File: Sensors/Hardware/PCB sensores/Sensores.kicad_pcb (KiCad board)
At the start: 2 copper layers, 108 x 129.5 mm, 49 parts, among them J1 Conn_01x02_Female, J2 Conn_01x03, J3 Conn_02x04_Top_Bottom, J4 Conn_01x02_Female, Q1 2N3904, U1 LM324, U2 LM324, U3 ADP1101, U4 MPX10DP, U5 LM358

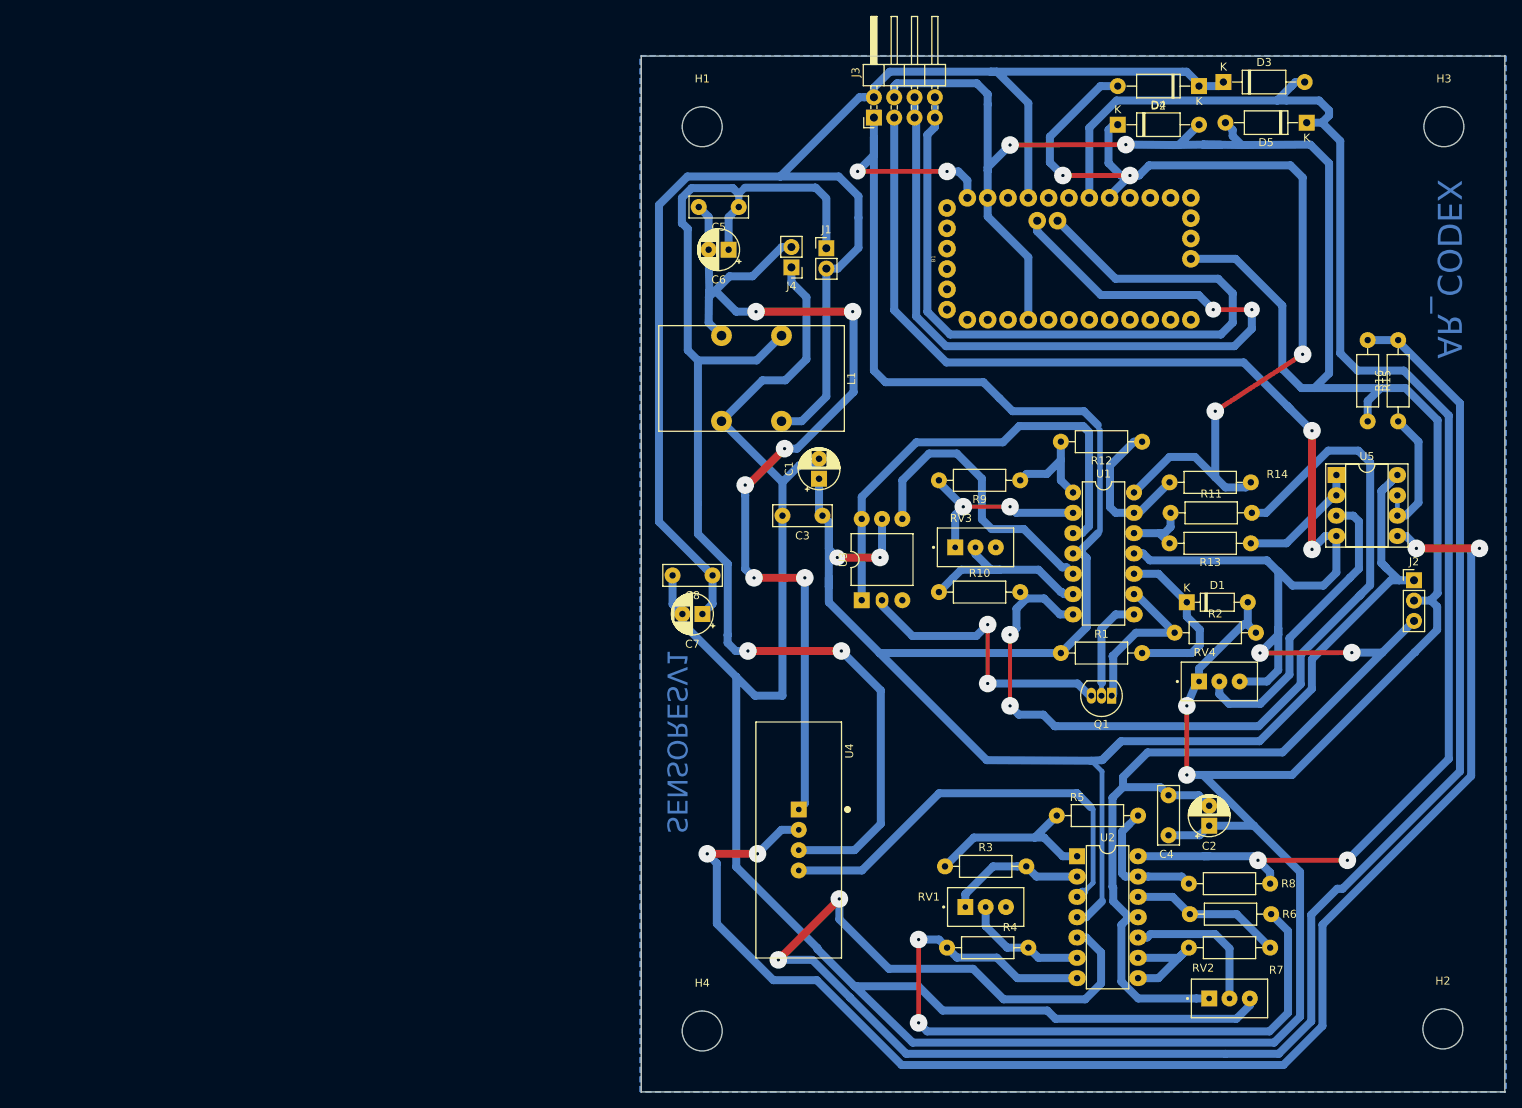
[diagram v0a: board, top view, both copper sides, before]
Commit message: Wrapping everything up. Sensors now work fine. Preliminary PID tunning.
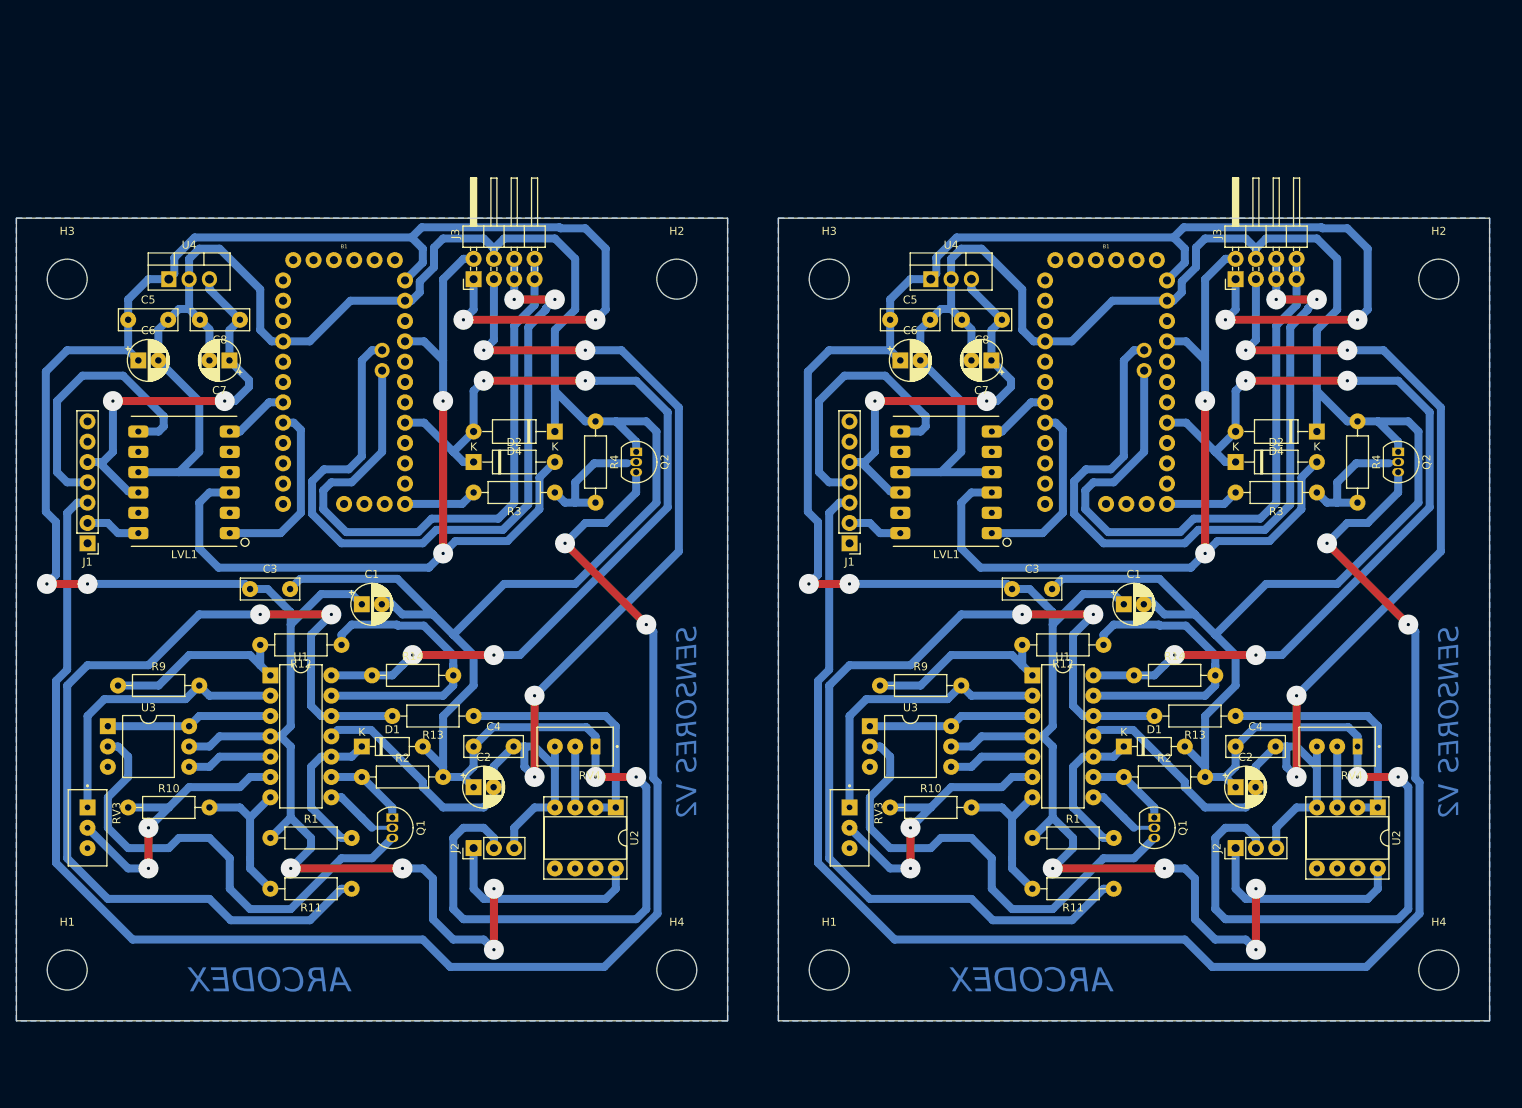
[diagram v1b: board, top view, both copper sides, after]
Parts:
- removed the B1 at (217.9, 43.2)
- removed the C1 at (186.7, 70.7)
- removed the C2 at (235.5, 114.0)
- removed the C3 at (187.1, 75.3)
- removed the C4 at (230.4, 115.2)
- removed the C5 at (176.7, 36.7)
- removed the C6 at (175.4, 42.0)
- removed the C7 at (172.1, 87.6)
- removed the C8 at (173.4, 82.8)
- removed the D1 at (232.7, 86.1)
- removed the D2 at (234.2, 21.6)
- removed D3, D5: DIODE, Diode_THT:D_A-405_P10.16mm_Horizontal
- removed the D4 at (224.0, 26.4)
- removed the H1 at (172.1, 26.7)
- removed the H2 at (264.7, 139.4)
- removed the H3 at (264.8, 26.7)
- removed the H4 at (172.1, 139.7)
- removed the J1 at (187.6, 41.9)
- removed the J2 at (261.1, 83.4)
- removed the J3 at (193.5, 25.5)
- removed J4: Conn_01x02_Female, Connector_PinHeader_2.54mm:PinHeader_1x02_P2.54mm_Vertical
- removed L1: L_Core_Ferrite_Coupled, I_Common_M:L_CommonMode_Wuerth_WE-CMB-M
- removed the Q1 at (223.3, 97.8)
- removed the R1 at (216.9, 92.5)
- removed the R10 at (201.7, 84.8)
- removed the R11 at (230.6, 74.9)
- removed the R12 at (227.1, 66.0)
- removed the R13 at (240.7, 78.7)
- removed the R14 at (240.7, 71.1)
- removed R15: 1M, Resistor_THT:R_Axial_DIN0207_L6.3mm_D2.5mm_P10.16mm_Horizontal
- removed R16: 5k1, Resistor_THT:R_Axial_DIN0207_L6.3mm_D2.5mm_P10.16mm_Horizontal
- removed the R2 at (231.1, 89.9)
- removed the R3 at (202.4, 119.1)
- removed the R4 at (212.9, 129.3)
- removed R5, R6, R7, R8: 10k, Resistor_THT:R_Axial_DIN0207_L6.3mm_D2.5mm_P10.16mm_Horizontal
- removed the R9 at (211.8, 70.9)
- removed RV1: 5k, 3296W-1-254LF:TRIM_3296W-1-254LF
- removed RV2: 100k, 3296W-1-254LF:TRIM_3296W-1-254LF
- removed the RV3 at (206.2, 79.2)
- removed the RV4 at (236.7, 96.0)
- removed the U1 at (218.4, 72.4)
- removed the U2 at (218.9, 117.9)
- removed the U3 at (192.0, 85.9)
- removed the U4 at (184.2, 115.8)
- removed U5: LM358, Package_DIP:DIP-8_W7.62mm_Socket
- added B1: ARDUINO_PRO_MINI, ARDUINO_PRO_MINI:ARDUINO_PRO_MINI, F.Cu at (127.3, 58.6)
- added B1: ARDUINO_PRO_MINI, ARDUINO_PRO_MINI:ARDUINO_PRO_MINI, F.Cu at (222.6, 58.6)
- added C1: CP, Capacitor_THT:CP_Radial_D5.0mm_P2.50mm, F.Cu at (129.5, 86.4)
- added C1: CP, Capacitor_THT:CP_Radial_D5.0mm_P2.50mm, F.Cu at (224.8, 86.4)
- added C2: CP, Capacitor_THT:CP_Radial_D5.0mm_P2.50mm, F.Cu at (143.5, 109.2)
- added C2: CP, Capacitor_THT:CP_Radial_D5.0mm_P2.50mm, F.Cu at (238.8, 109.2)
- added C3: C, Capacitor_THT:C_Rect_L7.2mm_W2.5mm_P5.00mm_FKS2_FKP2_MKS2_MKP2, F.Cu at (115.6, 84.5)
- added C3: C, Capacitor_THT:C_Rect_L7.2mm_W2.5mm_P5.00mm_FKS2_FKP2_MKS2_MKP2, F.Cu at (210.8, 84.5)
- added C4: C, Capacitor_THT:C_Rect_L7.2mm_W2.5mm_P5.00mm_FKS2_FKP2_MKS2_MKP2, F.Cu at (143.5, 104.1)
- added C4: C, Capacitor_THT:C_Rect_L7.2mm_W2.5mm_P5.00mm_FKS2_FKP2_MKS2_MKP2, F.Cu at (238.8, 104.1)
- added C5: C, Capacitor_THT:C_Rect_L7.2mm_W2.5mm_P5.00mm_FKS2_FKP2_MKS2_MKP2, F.Cu at (100.3, 50.8)
- added C5: C, Capacitor_THT:C_Rect_L7.2mm_W2.5mm_P5.00mm_FKS2_FKP2_MKS2_MKP2, F.Cu at (195.6, 50.8)
- added C6: CP, Capacitor_THT:CP_Radial_D5.0mm_P2.50mm, F.Cu at (101.6, 55.9)
- added C6: CP, Capacitor_THT:CP_Radial_D5.0mm_P2.50mm, F.Cu at (196.8, 55.9)
- added C7: CP, Capacitor_THT:CP_Radial_D5.0mm_P2.50mm, F.Cu at (113.0, 55.9)
- added C7: CP, Capacitor_THT:CP_Radial_D5.0mm_P2.50mm, F.Cu at (208.2, 55.9)
- added C8: C, Capacitor_THT:C_Rect_L7.2mm_W2.5mm_P5.00mm_FKS2_FKP2_MKS2_MKP2, F.Cu at (114.3, 50.8)
- added C8: C, Capacitor_THT:C_Rect_L7.2mm_W2.5mm_P5.00mm_FKS2_FKP2_MKS2_MKP2, F.Cu at (209.6, 50.8)
- added D1: D_Zener_2.2V, Diode_THT:D_DO-35_SOD27_P7.62mm_Horizontal, F.Cu at (129.5, 104.1)
- added D1: D_Zener_2.2V, Diode_THT:D_DO-35_SOD27_P7.62mm_Horizontal, F.Cu at (224.8, 104.1)
- added D2: DIODE, Diode_THT:D_A-405_P10.16mm_Horizontal, F.Cu at (143.5, 68.6)
- added D2: DIODE, Diode_THT:D_A-405_P10.16mm_Horizontal, F.Cu at (238.8, 68.6)
- added D4: DIODE, Diode_THT:D_A-405_P10.16mm_Horizontal, F.Cu at (153.7, 64.8)
- added D4: DIODE, Diode_THT:D_A-405_P10.16mm_Horizontal, F.Cu at (248.9, 64.8)
- added H1: MountingHole, MountingHole:MountingHole_5mm, F.Cu at (92.7, 132.1)
- added H1: MountingHole, MountingHole:MountingHole_5mm, F.Cu at (188.0, 132.1)
- added H2: MountingHole, MountingHole:MountingHole_5mm, F.Cu at (168.9, 45.7)
- added H2: MountingHole, MountingHole:MountingHole_5mm, F.Cu at (264.2, 45.7)
- added H3: MountingHole, MountingHole:MountingHole_5mm, F.Cu at (92.7, 45.7)
- added H3: MountingHole, MountingHole:MountingHole_5mm, F.Cu at (188.0, 45.7)
- added H4: MountingHole, MountingHole:MountingHole_5mm, F.Cu at (168.9, 132.1)
- added H4: MountingHole, MountingHole:MountingHole_5mm, F.Cu at (264.2, 132.1)
- added J1: SFM3300_CONN, SFM3300:PinHeader_1x07_P2.54mm_Vertical, F.Cu at (95.2, 78.7)
- added J1: SFM3300_CONN, SFM3300:PinHeader_1x07_P2.54mm_Vertical, F.Cu at (190.5, 78.7)
- added J2: Conn_01x03, Connector_PinHeader_2.54mm:PinHeader_1x03_P2.54mm_Vertical, F.Cu at (143.5, 116.8)
- added J2: Conn_01x03, Connector_PinHeader_2.54mm:PinHeader_1x03_P2.54mm_Vertical, F.Cu at (238.8, 116.8)
- added J3: Conn_02x04_Top_Bottom, Connector_PinHeader_2.54mm:PinHeader_2x04_P2.54mm_Horizontal, F.Cu at (143.5, 45.7)
- added J3: Conn_02x04_Top_Bottom, Connector_PinHeader_2.54mm:PinHeader_2x04_P2.54mm_Horizontal, F.Cu at (238.8, 45.7)
- added LVL1: Logic_LevelShifter, Level_Shifter:Logic_LevelShifter, F.Cu at (107.3, 78.1)
- added LVL1: Logic_LevelShifter, Level_Shifter:Logic_LevelShifter, F.Cu at (202.6, 78.1)
- added Q1: 2N3904, Package_TO_SOT_THT:TO-92_Inline, F.Cu at (133.3, 113.0)
- added Q1: 2N3904, Package_TO_SOT_THT:TO-92_Inline, F.Cu at (228.6, 113.0)
- added Q2: 2N7000, Package_TO_SOT_THT:TO-92_Inline, F.Cu at (163.8, 67.3)
- added Q2: 2N7000, Package_TO_SOT_THT:TO-92_Inline, F.Cu at (259.1, 67.3)
- added R1: 2k2, Resistor_THT:R_Axial_DIN0207_L6.3mm_D2.5mm_P10.16mm_Horizontal, F.Cu at (118.1, 115.6)
- added R1: 2k2, Resistor_THT:R_Axial_DIN0207_L6.3mm_D2.5mm_P10.16mm_Horizontal, F.Cu at (213.4, 115.6)
- added R10: 10k, Resistor_THT:R_Axial_DIN0207_L6.3mm_D2.5mm_P10.16mm_Horizontal, F.Cu at (100.3, 111.8)
- added R10: 10k, Resistor_THT:R_Axial_DIN0207_L6.3mm_D2.5mm_P10.16mm_Horizontal, F.Cu at (195.6, 111.8)
- added R11: 10k, Resistor_THT:R_Axial_DIN0207_L6.3mm_D2.5mm_P10.16mm_Horizontal, F.Cu at (128.3, 121.9)
- added R11: 10k, Resistor_THT:R_Axial_DIN0207_L6.3mm_D2.5mm_P10.16mm_Horizontal, F.Cu at (223.5, 121.9)
- added R12: 10k, Resistor_THT:R_Axial_DIN0207_L6.3mm_D2.5mm_P10.16mm_Horizontal, F.Cu at (127.0, 91.4)
- added R12: 10k, Resistor_THT:R_Axial_DIN0207_L6.3mm_D2.5mm_P10.16mm_Horizontal, F.Cu at (222.2, 91.4)
- added R13: 10k, Resistor_THT:R_Axial_DIN0207_L6.3mm_D2.5mm_P10.16mm_Horizontal, F.Cu at (143.5, 100.3)
- added R13: 10k, Resistor_THT:R_Axial_DIN0207_L6.3mm_D2.5mm_P10.16mm_Horizontal, F.Cu at (238.8, 100.3)
- added R14: 10k, Resistor_THT:R_Axial_DIN0207_L6.3mm_D2.5mm_P10.16mm_Horizontal, F.Cu at (130.8, 95.2)
- added R14: 10k, Resistor_THT:R_Axial_DIN0207_L6.3mm_D2.5mm_P10.16mm_Horizontal, F.Cu at (226.1, 95.2)
- added R2: 1k5, Resistor_THT:R_Axial_DIN0207_L6.3mm_D2.5mm_P10.16mm_Horizontal, F.Cu at (129.5, 108.0)
- added R2: 1k5, Resistor_THT:R_Axial_DIN0207_L6.3mm_D2.5mm_P10.16mm_Horizontal, F.Cu at (224.8, 108.0)
- added R3: 1k, Resistor_THT:R_Axial_DIN0207_L6.3mm_D2.5mm_P10.16mm_Horizontal, F.Cu at (153.7, 72.4)
- added R3: 1k, Resistor_THT:R_Axial_DIN0207_L6.3mm_D2.5mm_P10.16mm_Horizontal, F.Cu at (248.9, 72.4)
- added R4: 100k, Resistor_THT:R_Axial_DIN0207_L6.3mm_D2.5mm_P10.16mm_Horizontal, F.Cu at (158.8, 63.5)
- added R4: 100k, Resistor_THT:R_Axial_DIN0207_L6.3mm_D2.5mm_P10.16mm_Horizontal, F.Cu at (254.0, 63.5)
- added R9: 10k, Resistor_THT:R_Axial_DIN0207_L6.3mm_D2.5mm_P10.16mm_Horizontal, F.Cu at (99.1, 96.5)
- added R9: 10k, Resistor_THT:R_Axial_DIN0207_L6.3mm_D2.5mm_P10.16mm_Horizontal, F.Cu at (194.3, 96.5)
- added RV3: 5k, 3296W-1-254LF:TRIM_3296W-1-254LF, F.Cu at (95.2, 114.3)
- added RV3: 5k, 3296W-1-254LF:TRIM_3296W-1-254LF, F.Cu at (190.5, 114.3)
- added RV4: 100k, 3296W-1-254LF:TRIM_3296W-1-254LF, F.Cu at (156.2, 104.1)
- added RV4: 100k, 3296W-1-254LF:TRIM_3296W-1-254LF, F.Cu at (251.5, 104.1)
- added U1: LM324, Package_DIP:DIP-14_W7.62mm, F.Cu at (118.1, 95.2)
- added U1: LM324, Package_DIP:DIP-14_W7.62mm, F.Cu at (213.4, 95.2)
- added U2: LM358, Package_DIP:DIP-8_W7.62mm_Socket, F.Cu at (161.3, 111.8)
- added U2: LM358, Package_DIP:DIP-8_W7.62mm_Socket, F.Cu at (256.5, 111.8)
- added U3: ADP1101, 3296W-1-254LF:DIP-6_W10.16mm, F.Cu at (97.8, 101.6)
- added U3: ADP1101, 3296W-1-254LF:DIP-6_W10.16mm, F.Cu at (193.0, 101.6)
- added U4: LM358, Package_TO_SOT_THT:TO-220-3_Vertical, F.Cu at (105.4, 45.7)
- added U4: LM358, Package_TO_SOT_THT:TO-220-3_Vertical, F.Cu at (200.7, 45.7)
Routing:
- net (no net): track 0.00 -> 1998.4 mm, vias 0 -> 30
- net Net-(R15-Pad1): track 232.1 -> 0.00 mm, vias 2 -> 0
- net GND: track 567.7 -> 351.2 mm, vias 4 -> 2
- net /GND_SFM3300: track 0.00 -> 195.7 mm, vias 0 -> 2
- net /A1:MPX10DP: track 187.4 -> 0.00 mm, vias 2 -> 0
- net +OutputMPX10DP: track 186.2 -> 0.00 mm, vias 4 -> 0
- net +3.3VA: track 153.4 -> 0.00 mm, vias 2 -> 0
- net GNDA: track 125.3 -> 0.00 mm, vias 6 -> 0
- net -12V: track 267.6 -> 150.2 mm
- net Net-(R11-Pad1): track 8.46 -> 121.9 mm, vias 0 -> 2
- net Net-(R10-Pad2): track 113.8 -> 19.1 mm, vias 2 -> 0
- net Net-(R4-Pad2): track 93.9 -> 0.00 mm, vias 2 -> 0
- net +3V3: track 197.9 -> 109.0 mm, vias 0 -> 2
- net -OutputMPX10DP: track 56.0 -> 0.00 mm
- net +5V: track 0.00 -> 52.3 mm, vias 0 -> 2
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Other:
- board size 108 x 129.5 mm -> 184.1 x 100.3 mm
- net class Default: via_dia 3 -> 2.5
- board text added: "ARCODEX"
- board text added: "SENSORES V2"
- board text removed: "AR_CODEX"
- board text removed: "SENSORESV1"
